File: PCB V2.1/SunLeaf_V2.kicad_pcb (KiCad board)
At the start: 4 copper layers, 77.5 x 40 mm, 157 parts, among them IC1 ESP_09, J1 20021121-00010C4LF, J10 B4B-PH-K-S(LF)(SN), J11 B4B-PH-K-S(LF)(SN), J12 B4B-PH-K-S(LF)(SN), J13 B4B-PH-K-S(LF)(SN), J14 B4B-PH-K-S(LF)(SN), J15 B4B-PH-K-S(LF)(SN), J16 B4B-PH-K-S(LF)(SN), J2 0475890001-MicroUSBPort, J3 B2B-PH-K-S(LF)(SN), J4 B3B-PH-K-S(LF)(SN), J5 B4B-PH-K-S(LF)(SN), J6 B4B-PH-K-S(LF)(SN), J7 B4B-PH-K-S(LF)(SN), J8 B4B-PH-K-S(LF)(SN), J9 B4B-PH-K-S(LF)(SN), P2 CONN_01X03, Q1 DMG2307L-7, Q2 DMG2307L-7, SW1 B3U-1000P, SW2 B3U-1000P, T1 1909763-1, U1 STM32F446RET6_-_TQFP64, U2 BQ24210DQCT, U3 AZ1117CR-3.3TRG1_1, U4 74HC4052D, U5 PCA9518DBQR, X1 ABM3B8.000MHZB2T, X2 ABS07-32.768KHZ-9-T

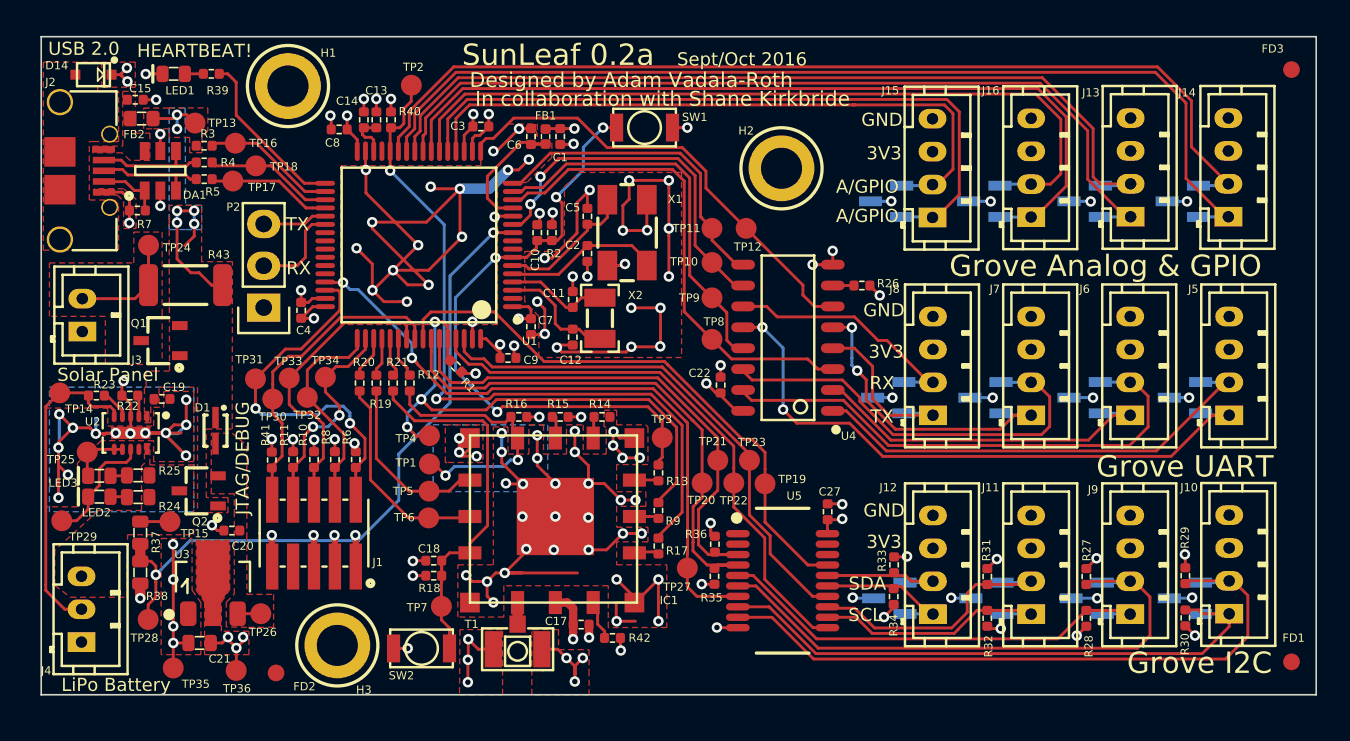
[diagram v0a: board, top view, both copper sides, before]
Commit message: LDO and Switch
LDO swapped out for one that better matches the complete system's
amperage requirements. The LDO is now a 600mA one and has a toggle
switch for shuttingit on and off, this will allow the SunLeaf to be
stored and or shipped.
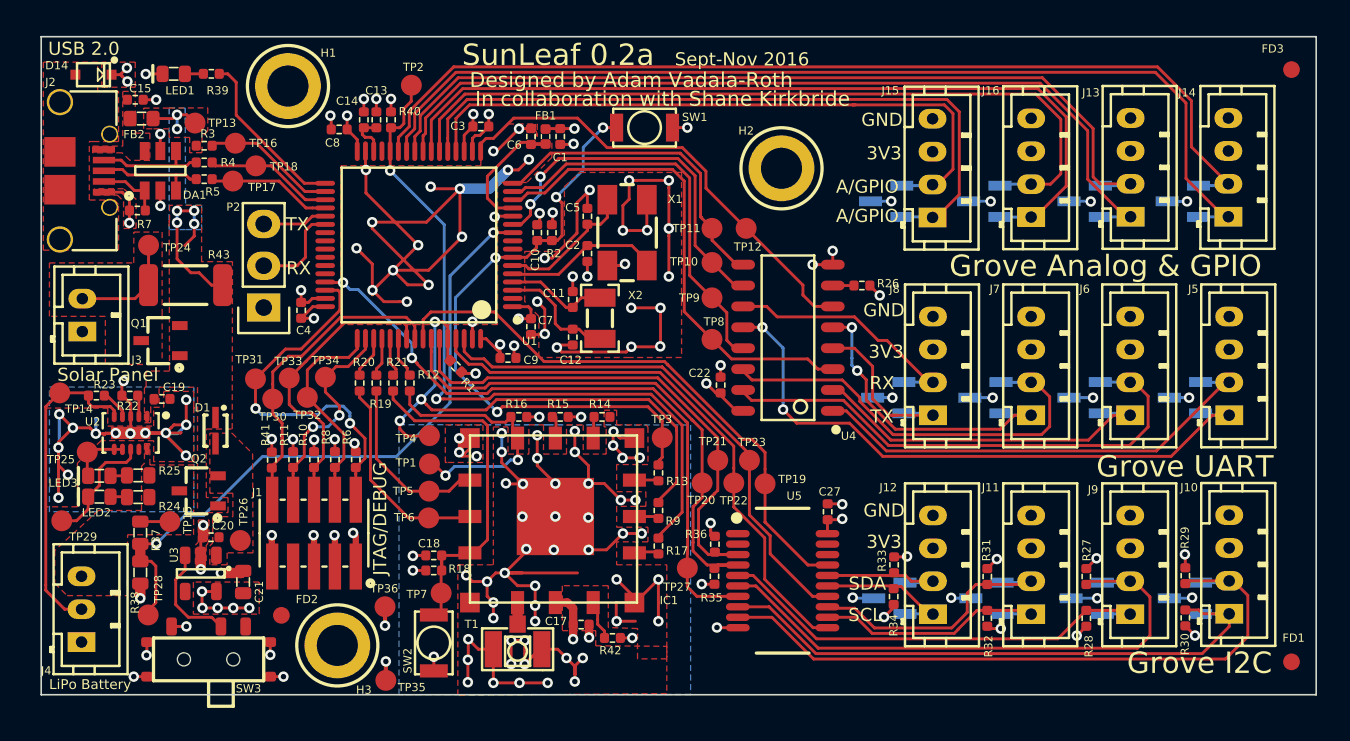
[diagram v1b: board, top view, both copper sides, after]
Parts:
- added SW3: CUS-12TB, PCB_Footprints:CUS-12TB, F.Cu at (53.2, 67.8)
- U3: value AZ1117CR-3.3TRG1_1 -> AP2112K-3.3TRG1; footprint PCB_Footprints:AZ1117CR-3.3TRG1 -> PCB_Footprints:AP2112K-3.3TRG1
- moved TP35 12.9 mm to (64.0, 69.1), turned to 180 degrees
- moved TP36 9.84 mm to (63.9, 64.7), turned to 180 degrees
- moved TP26 4.62 mm to (55.1, 60.6)
- moved C21 4.55 mm to (55.3, 63.1), turned to 90 degrees
- moved FD2 3.52 mm to (57.6, 65.2)
- moved C20 1.32 mm to (53.3, 60.4)
- moved U3 0.95 mm to (52.7, 62.6), turned to 270 degrees
- moved SW2 0.82 mm to (66.9, 66.9), turned to 270 degrees
- moved TP7 0.81 mm to (67.3, 63.8)
- moved C18 0.32 mm to (66.9, 61.5)
- moved R18 0.32 mm to (66.9, 62.4)
- moved TP28 0.27 mm to (49.5, 65.2)
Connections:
- U3 pad 1: GND -> Net-(C20-Pad1)
- U3 pad 2: +3V3 -> GND
- U3 pad 3: Net-(C20-Pad1) -> Net-(SW3-Pad2)
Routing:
- net GND: track 257.7 -> 273.4 mm, vias 136 -> 151
- net Net-(SW3-Pad2): track 0.00 -> 6.54 mm
- net Net-(C18-Pad1): track 24.8 -> 23.0 mm
- net +3V3: track 45.2 -> 47.0 mm, vias 34 -> 37
- net /MCU-STM32F446RET6/BAT_VOLT: track 42.0 -> 40.6 mm
- net Net-(C20-Pad1): track 1.41 -> 0.00 mm
- net /MCU-STM32F446RET6/ESPTOST_BOOT0: track 33.4 -> 34.1 mm
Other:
- board text added: "Sept-Nov 2016"
- board text removed: "HEARTBEAT!"
- board text removed: "Sept/Oct 2016"

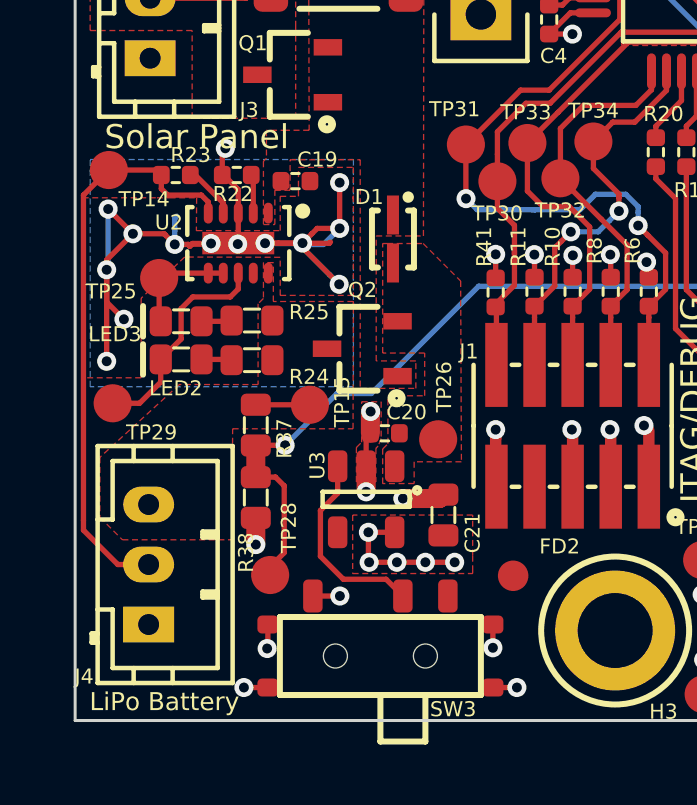
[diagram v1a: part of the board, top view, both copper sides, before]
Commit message: Diode Error
The pin numbering on the footprint for the diode in the LDO input source
switching circiut was revered, it has now been adjusted to be correct.
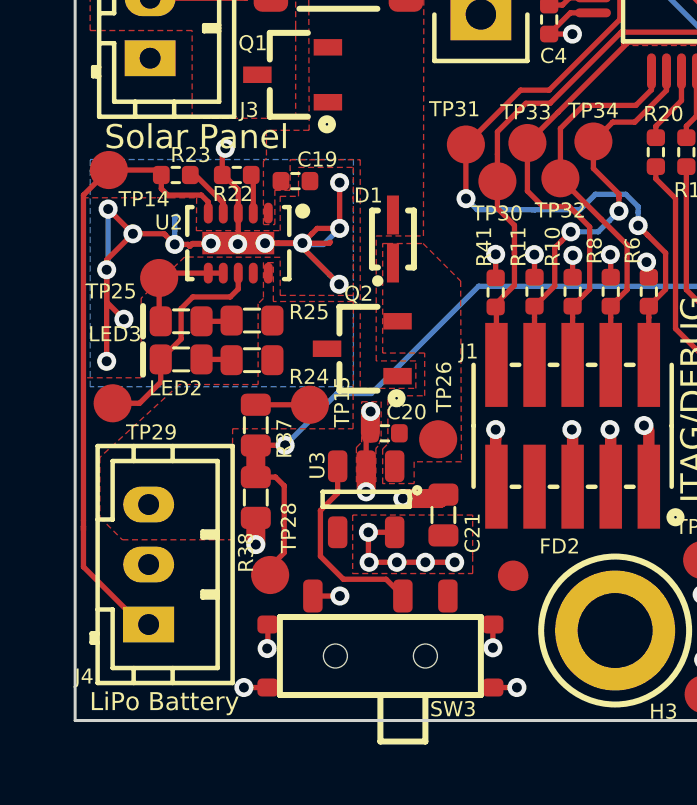
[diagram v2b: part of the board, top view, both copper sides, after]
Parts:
- turned D1 to 90 degrees
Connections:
- J4 pad 1: GND -> /Power-System/THERM
- J4 pad 2: /Power-System/THERM -> GND
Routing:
- net /Power-System/THERM: track 19.6 -> 21.2 mm
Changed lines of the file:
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@@
   (general
     (links 347)
-    (no_connects 1)
+    (no_connects 0)
     (area 42.949999 29.949999 120.550001 70.050001)
     (thickness 1.6)
     (drawings 157)
-    (tracks 1511)
+    (tracks 1513)
     (zones 0)
     (modules 158)
@@
   )
   (setup
-    (last_trace_width 0.635)
+    (last_trace_width 0.1778)
     (user_trace_width 0.1778)
     (user_trace_width 0.254)
@@
     (diff_pair_width 0.1778)
   )
+  (module PCB_Footprints:BAT20JFILM (layer F.Cu)
+    (at 53.594 53.9496 90)
+    (fp_text reference D1 (at 1.4496 -0.819 180) (layer F.SilkS)
+      (effects (font (size 0.5 0.5) (thickness 0.1)))
+    )
+    (fp_text value BAT20JFILM (at 0 2.032 90) (layer F.Fab)
+      (effects (font (size 0.5 0.5) (thickness 0.1)))
+    )
+    (fp_line (start -0.95 -0.5) (end -0.95 -0.7) (layer F.SilkS) (width 0.2))
+    (fp_line (start 0.95 -0.7) (end -0.95 -0.7) (layer F.SilkS) (width 0.2))
+    (fp_line (start 0.95 -0.5) (end 0.95 -0.7) (layer F.SilkS) (width 0.2))
+    (fp_line (start -0.95 0.7) (end 0.95 0.7) (layer F.SilkS) (width 0.2))
+    (fp_line (start -0.95 0.5) (end -0.95 0.7) (layer F.SilkS) (width 0.2))
+    (fp_line (start 0.95 0.5) (end 0.95 0.7) (layer F.SilkS) (width 0.2))
+    (fp_line (start 0 -0.381) (end 0 0.381) (layer Dwgs.User) (width 0.05))
+    (fp_line (start 0.127 0) (end -0.127 0) (layer Dwgs.User) (width 0.05))
+    (fp_line (start -1.651 -1.016) (end 1.651 -1.016) (layer Dwgs.User) (width 0.05))
+    (fp_line (start -1.651 1.016) (end -1.651 -1.016) (layer Dwgs.User) (width 0.05))
+    (fp_line (start 1.651 1.016) (end -1.651 1.016) (layer Dwgs.User) (width 0.05))
+    (fp_line (start 1.651 -1.016) (end 1.651 1.016) (layer Dwgs.User) (width 0.05))
+    (fp_circle (center -1.397 -0.508) (end -1.3335 -0.4445) (layer F.SilkS) (width 0.2))
+    (pad 2 smd rect (at -0.8 0 90) (size 1.3 0.4) (layers F.Cu F.Paste F.Mask)
+      (net 12 "Net-(C20-Pad1)") (solder_mask_margin 0.102))
+    (pad 1 smd rect (at 0.8 0 90) (size 1.3 0.4) (layers F.Cu F.Paste F.Mask)
+      (net 13 /MCU-STM32F446RET6/VBUS) (solder_mask_margin 0.102))
+    (model C:/Users/adam/Documents/GitHub/footprints/3D/VRML/SOD-323.wrl
+      (at (xyz -0.03543307086614173 -0.007874015748031498 0.02165354330708662))
+      (scale (xyz 0.37 0.37 0.4))
+      (rotate (xyz -90 0 180))
+    )
+  )
   (module PCB_Footprints:AP2112K-3.3TRG1 (layer F.Cu)
     (at 52.7 62.625 270)
@@
   (module PCB_Footprints:TEST_POINT (layer F.Cu)
     (at 63.95 69.125 180)
-    (fp_text reference TP35 (at -1.575 -0.425 360) (layer F.SilkS)
+    (fp_text reference TP35 (at -1.575 -0.425) (layer F.SilkS)
       (effects (font (size 0.5 0.5) (thickness 0.1)))
     )
@@
     )
   )
-  (module PCB_Footprints:BAT20JFILM (layer F.Cu)
-    (at 53.594 53.9496 270)
-    (fp_text reference D1 (at -1.3996 0.794) (layer F.SilkS)
-      (effects (font (size 0.5 0.5) (thickness 0.1)))
-    )
-    (fp_text value BAT20JFILM (at 0 2.032 270) (layer F.Fab)
-      (effects (font (size 0.5 0.5) (thickness 0.1)))
-    )
-    (fp_line (start -0.95 -0.5) (end -0.95 -0.7) (layer F.SilkS) (width 0.2))
-    (fp_line (start 0.95 -0.7) (end -0.95 -0.7) (layer F.SilkS) (width 0.2))
-    (fp_line (start 0.95 -0.5) (end 0.95 -0.7) (layer F.SilkS) (width 0.2))
-    (fp_line (start -0.95 0.7) (end 0.95 0.7) (layer F.SilkS) (width 0.2))
-    (fp_line (start -0.95 0.5) (end -0.95 0.7) (layer F.SilkS) (width 0.2))
-    (fp_line (start 0.95 0.5) (end 0.95 0.7) (layer F.SilkS) (width 0.2))
-    (fp_line (start 0 -0.381) (end 0 0.381) (layer Dwgs.User) (width 0.05))
-    (fp_line (start 0.127 0) (end -0.127 0) (layer Dwgs.User) (width 0.05))
-    (fp_line (start -1.651 -1.016) (end 1.651 -1.016) (layer Dwgs.User) (width 0.05))
-    (fp_line (start -1.651 1.016) (end -1.651 -1.016) (layer Dwgs.User) (width 0.05))
-    (fp_line (start 1.651 1.016) (end -1.651 1.016) (layer Dwgs.User) (width 0.05))
-    (fp_line (start 1.651 -1.016) (end 1.651 1.016) (layer Dwgs.User) (width 0.05))
-    (fp_circle (center -1.397 -0.508) (end -1.3335 -0.4445) (layer F.SilkS) (width 0.2))
-    (pad 1 smd rect (at -0.8 0 270) (size 1.3 0.4) (layers F.Cu F.Paste F.Mask)
-      (net 13 /MCU-STM32F446RET6/VBUS) (solder_mask_margin 0.102))
-    (pad 2 smd rect (at 0.8 0 270) (size 1.3 0.4) (layers F.Cu F.Paste F.Mask)
-      (net 12 "Net-(C20-Pad1)") (solder_mask_margin 0.102))
-    (model C:/Users/adam/Documents/GitHub/footprints/3D/VRML/SOD-323.wrl
-      (at (xyz -0.03543307086614173 -0.007874015748031498 0.02165354330708662))
-      (scale (xyz 0.37 0.37 0.4))
-      (rotate (xyz -90 0 180))
-    )
-  )
   (module "PCB_Footprints:B4B-PH-K-S(LF)(SN)" (layer F.Cu)
     (at 103.1748 65.1002 90)
@@
   (module PCB_Footprints:DMG2307L-7 (layer F.Cu)
     (at 52.5714 57.6066 180)
-    (fp_text reference Q2 (at -0.0036 1.9566 180) (layer F.SilkS)
+    (fp_text reference Q2 (at 0.1214 1.8316 180) (layer F.SilkS)
       (effects (font (size 0.5 0.5) (thickness 0.1)))
     )
@@
     (fp_line (start -1.95 2.8) (end -1.95 -1.7) (layer F.SilkS) (width 0.15))
     (pad 1 thru_hole rect (at 0 0 90) (size 1.2 1.7) (drill 0.7) (layers *.Cu *.Mask F.SilkS)
-      (net 2 GND))
-    (pad 2 thru_hole oval (at 2 0 90) (size 1.2 1.7) (drill 0.7) (layers *.Cu *.Mask F.SilkS)
       (net 50 /Power-System/THERM))
+    (pad 2 thru_hole oval (at 2 0 90) (size 1.2 1.7) (drill 0.7) (layers *.Cu *.Mask F.SilkS)
+      (net 2 GND))
     (pad 3 thru_hole oval (at 4 0 90) (size 1.2 1.7) (drill 0.7) (layers *.Cu *.Mask F.SilkS)
       (net 49 /Power-System/BAT))
@@
   (segment (start 50.825 59.475) (end 49.024 59.475) (width 0.1778) (layer F.Cu) (net 49))
   (segment (start 49.024 59.475) (end 49.022 59.473) (width 0.1778) (layer F.Cu) (net 49))
+  (segment (start 43.276934 63.525) (end 43.276934 63.325) (width 0.1778) (layer F.Cu) (net 50))
+  (segment (start 43.276934 63.654734) (end 43.276934 63.525) (width 0.1778) (layer F.Cu) (net 50))
+  (segment (start 43.276934 63.525) (end 43.276934 64.876934) (width 0.1778) (layer F.Cu) (net 50))
+  (segment (start 43.276934 64.876934) (end 45.2 66.8) (width 0.1778) (layer F.Cu) (net 50))
+  (segment (start 45.2 66.8) (end 45.45 66.8) (width 0.1778) (layer F.Cu) (net 50))
   (segment (start 43.276934 52.485008) (end 43.276934 63.325) (width 0.1778) (layer F.Cu) (net 50))
-  (segment (start 45.45 64.8) (end 44.4222 64.8) (width 0.1778) (layer F.Cu) (net 50))
-  (segment (start 44.4222 64.8) (end 43.276934 63.654734) (width 0.1778) (layer F.Cu) (net 50))
-  (segment (start 43.276934 63.654734) (end 43.276934 63.325) (width 0.1778) (layer F.Cu) (net 50))
   (segment (start 44.125 51.65) (end 44.111942 51.65) (width 0.1778) (layer F.Cu) (net 50))
   (segment (start 44.111942 51.65) (end 43.276934 52.485008) (width 0.1778) (layer F.Cu) (net 50))
